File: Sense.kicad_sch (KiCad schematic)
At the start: 35 parts, among them J1 22-28-8083, J2 1x3 pin vertical, J3 1x3 pin vertical, J4 1x3 pin vertical, J5 1x3 pin vertical, P1 5KEV-0, P2 5KEV-0, T1 NSI50010YT1G, U1 INA226

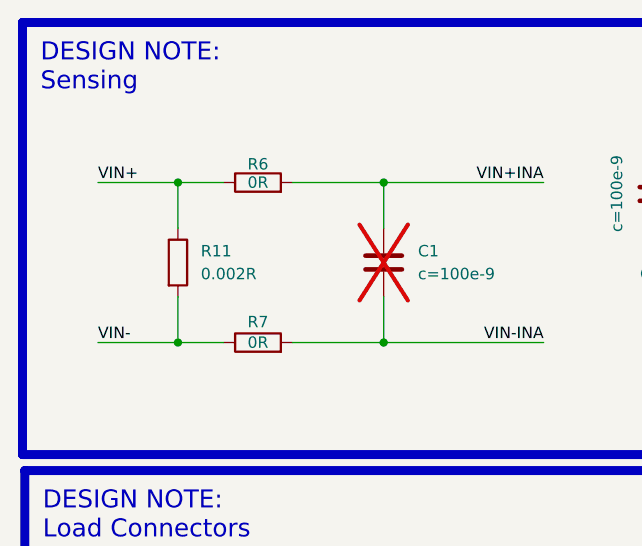
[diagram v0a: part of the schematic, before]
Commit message: Changed sense resistor and fixed connector position
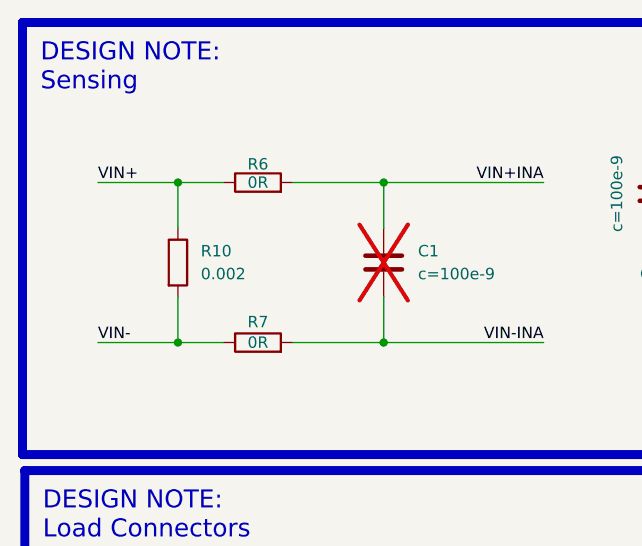
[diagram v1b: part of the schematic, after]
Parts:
- removed R11: 0.002R, Resistor_SMD:R_0805_2012Metric_Pad1.20x1.40mm_HandSolder, symbol 0_resistors:PMR10EZPFV2L00
- added R10: 0.002, Resistor_SMD:R_1206_3216Metric_Pad1.30x1.75mm_HandSolder, symbol 0_resistors:WSL12062L000FEA
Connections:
- net VIN+: now also R10.1
- net VIN-: now also R10.2
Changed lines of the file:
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@@
 			"AAAAAAAAAAAAAAAAAAAAAAAAAAAAAAAAAAAAAAAAAAAAAAAAAAAAAAAAAAAAAAAAAAAAAAAAAAAA"
 			"AAAAAAAAAAAAAAAAAAAAAAAAAAAAAAAAAAAAAAAAAAAAAAAAAAAAAAAAAAAAAAAAAAAAAAAAAAAA"
+			"AAAAAAAAAAAAAAAAAAAAAAAAAAAAAAAAAAAAAAAAAAAAAAAAAAAAAAAAAAAAAAAAAAAAAAAAAAAA"
+			"AAAAAAAAAAAAAAAAAAAAAAAAAAAAAAAAAAAAAAAAAAAAAAAAAAAAAAAAAAAAAAAAAAAAAAAAAAAA"
+			"AAAAAAAAAAAAAAAAAAAAAAAAAAAAAAAAAAAAAAAAAAAAAAAAAAAAAAAAAAAAAAAAAAAAAAAAAAAA"
+			"AAAAAAAAAAAAAAAAAAAAAAAAAAAAAAAAAAAAAAAAAAAAAAAAAAAAAAAAAAAAAAAAAAAAAAAAAAAA"
+			"AAAAAAAAAAAAAAAAAAAAAAAAAAAAAAAAAAAAAAAAAAAAAAAAAAAAAAAAAAAAAAAAAAAAAAAAAAAA"
+			"AAAAAAAAAAAAAAAAAAAAAAAAAAAAAAAAAAAAAAAAAAAAAAAAAAAAAAAAAAAAAAAAAAAAAAAAAAAA"
+			"AAAAAAAAAAAAAAAAAAAAAAAAAAAAAAAAAAAAAAAAAAAAAAAAAAAAAAAAAAAAAAAAAAAAAAAAAAAA"
+			"AAAAAAAAAAAAAAAAAAAAAAAAAAAAAAAAAAAAAAAAAAAAAAAAAAAAAAAAAAAAAAAAAAAAAAAAAAAA"
+			"AAAAAAAAAAAAAAAAAAAAAAAAAAAAAAAAAAAAAAAAAAAAAAAAAAAAAAAAAAAAAAAAAAAAAAAAAAAA"
+			"AAAAAAAAAAAAAAAAAAAAAAAAAAAAAAAAAAAAAAAAAAAAAAAAAAAAAAAAAAAAAAAAAAAAAAAAAAAA"
+			"AAAAAAAAAAAAAAAAAAAAAAAAAAAAAAAAAAAAAAAAAAAAAAAAAAAAAAAAAAAAAAAAAAAAAAAAAAAA"
+			"AAAAAAAAAAAAAAAAAAAAAAAAAAAAAAAAAAAAAAAAAAAAAAAAAAAAAAAAAAAAAAAAAAAAAAAAAAAA"
+			"AAAAAAAAAAAAAAAAAAAAAAAAAAAAAAAAAAAAAAAAAAAAAAAAAAAAAAAAAAAAAAAAAAAAAAAAAAAA"
+			"AAAAAAAAAAAAAAAAAAAAAAAAAAAAAAAAAAAAAAAAAAAAAAAAAAAAAAAAAAAAAAAAAAAAAAAAAAAA"
+			"AAAAAAAAAAAAAAAAAAAAAAAAAAAAAAAAAAAAAAAAAAAAAAAAAAAAAAAAAAAAAAAAAAAAAAAAAAAA"
+			"AAAAAAAAAAAAAAAAAAAAAAAAAAAAAAAAAAAAAAAAAAAAAAAAAAAAAAAAAAAAAAAAAAAAAAAAAAAA"
+			"AAAAAAAAAAAAAAAAAAAAAAAAAAAAAAAAAAAAAAAAAAAAAAAAAAAAAAAAAAAAAAAAAAAAAAAAAAAA"
+			"AAAAAAAAAAAAAAAAAAAAAAAAAAAAAAAAAAAAAAAAAAAAAAAAAAAAAAAAAAAAAAAAAAAAAAAAAAAA"
 			"AAAAAAAAAAAAAAAAAAAAAAAAAAAAAA=="
 		)
@@
 	)
 	(symbol
+		(lib_id "0_resistors:WSL12062L000FEA")
+		(at 31.75 40.64 0)
+		(unit 1)
+		(exclude_from_sim no)
+		(in_bom yes)
+		(on_board yes)
+		(dnp no)
+		(fields_autoplaced yes)
+		(property "Reference" "R10"
+			(at 34.29 39.3699 0)
+			(effects
+				(font
+					(size 1.27 1.27)
+				)
+				(justify left)
+			)
+		)
+		(property "Value" "0.002"
+			(at 34.29 41.9099 0)
+			(effects
+				(font
+					(size 1.27 1.27)
+				)
+				(justify left)
+			)
+		)
+		(property "Footprint" "Resistor_SMD:R_1206_3216Metric_Pad1.30x1.75mm_HandSolder"
+			(at 31.75 40.64 0)
+			(effects
+				(font
+					(size 1.27 1.27)
+				)
+				(hide yes)
+			)
+		)
+		(property "Datasheet" "https://www.vishay.com/doc?30100"
+			(at 31.75 40.64 0)
+			(effects
+				(font
+					(size 1.27 1.27)
+				)
+				(hide yes)
+			)
+		)
+		(property "Description" "Current Sense Resistor, 0.002R, 1206, SMD, 1/4watt, 1%"
+			(at 31.75 40.64 0)
+			(effects
+				(font
+					(size 1.27 1.27)
+				)
+				(hide yes)
+			)
+		)
+		(property "CompanyPN" ""
+			(at 31.75 40.64 0)
+			(effects
+				(font
+					(size 1.27 1.27)
+				)
+				(hide yes)
+			)
+		)
+		(property "Manufacturer Part Number" "WSL12062L000FEA"
+			(at 31.75 40.64 0)
+			(effects
+				(font
+					(size 1.27 1.27)
+				)
+				(hide yes)
+			)
+		)
+		(property "Sim.Device" "R"
+			(at 31.75 40.64 0)
+			(effects
+				(font
+					(size 1.27 1.27)
+				)
+				(hide yes)
+			)
+		)
+		(property "Sim.Pins" "1=+ 2=-"
+			(at 31.75 40.64 0)
+			(effects
+				(font
+					(size 1.27 1.27)
+				)
+				(hide yes)
+			)
+		)
+		(pin "2"
+		)
+		(pin "1"
+		)
+		(instances
+			(project ""
+				(path "/0650c7a8-acba-429c-9f8e-eec0baf0bc1c/fede4c36-00cc-4d3d-b71c-5243ba232202/7d5a1283-086b-46b0-8df7-a9850521fb5e"
+					(reference "R10")
+					(unit 1)
+				)
+			)
+		)
+	)
+	(symbol
 		(lib_id "power:VCC")
 		(at 246.38 115.57 0)
@@
 					(unit 1)
 				)
-			)
-		)
-	)
-	(symbol
-		(lib_id "0_resistors:PMR10EZPFV2L00")
-		(at 31.75 40.64 0)
-		(unit 1)
-		(exclude_from_sim no)
-		(in_bom yes)
-		(on_board yes)
-		(dnp no)
-		(fields_autoplaced yes)
-		(property "Reference" "R11"
-			(at 34.29 39.3699 0)
-			(effects
-				(font
-					(size 1.27 1.27)
-				)
-				(justify left)
-			)
-		)
-		(property "Value" "0.002R"
-			(at 34.29 41.9099 0)
-			(effects
-				(font
-					(size 1.27 1.27)
-				)
-				(justify left)
-			)
-		)
-		(property "Footprint" "Resistor_SMD:R_0805_2012Metric_Pad1.20x1.40mm_HandSolder"
-			(at 31.75 40.64 0)
-			(effects
-				(font
-					(size 1.27 1.27)
-				)
-				(hide yes)
-			)
-		)
-		(property "Datasheet" "https://fscdn.rohm.com/en/products/databook/datasheet/passive/resistor/chip_resistor/pmr_series-e.pdf"
-			(at 31.75 40.64 0)
-			(effects
-				(font
-					(size 1.27 1.27)
-				)
-				(hide yes)
-			)
-		)
-		(property "Description" "RESISTOR, 0.002R, 1%, 1/2W 0805"
-			(at 31.75 40.64 0)
-			(effects
-				(font
-					(size 1.27 1.27)
-				)
-				(hide yes)
-			)
-		)
-		(property "CompanyPN" ""
-			(at 31.75 40.64 0)
-			(effects
-				(font
-					(size 1.27 1.27)
-				)
-				(hide yes)
-			)
-		)
-		(property "Sim.Pins" "1=+ 2=-"
-			(at 31.75 40.64 0)
-			(effects
-				(font
-					(size 1.27 1.27)
-				)
-				(hide yes)
-			)
-		)
-		(property "Manufacturer Parn Number" "PMR10EZPFV2L00"
-			(at 31.75 40.64 0)
-			(effects
-				(font
-					(size 1.27 1.27)
-				)
-				(hide yes)
-			)
-		)
-		(property "Sim.Device" "R"
-			(at 31.75 40.64 0)
-			(effects
-				(font
-					(size 1.27 1.27)
-				)
-				(hide yes)
-			)
-		)
-		(property "Sim.Params" "r=0.002"
-			(at 31.75 40.64 0)
-			(effects
-				(font
-					(size 1.27 1.27)
-				)
-				(hide yes)
-			)
-		)
-		(property "Manufacturer Part Number" "CRCW060333R0FKEA"
-			(at 31.75 40.64 0)
-			(effects
-				(font
-					(size 1.27 1.27)
-				)
-				(hide yes)
-			)
-		)
-		(pin "1"
-		)
-		(pin "2"
-		)
-		(instances
-			(project ""
-				(path "/0650c7a8-acba-429c-9f8e-eec0baf0bc1c/fede4c36-00cc-4d3d-b71c-5243ba232202/7d5a1283-086b-46b0-8df7-a9850521fb5e"
-					(reference "R11")
-					(unit 1)
-				)

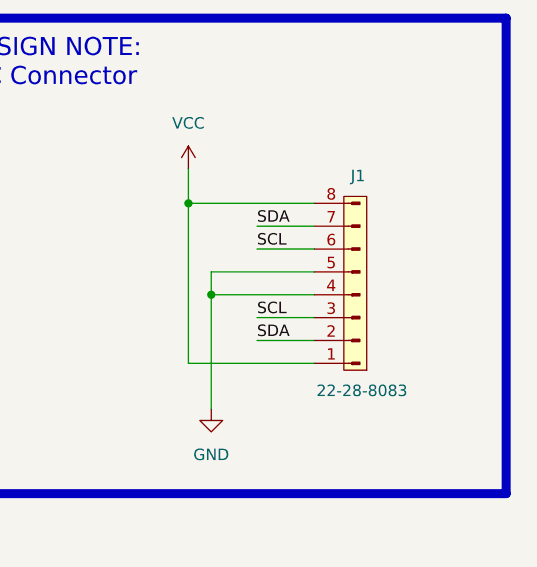
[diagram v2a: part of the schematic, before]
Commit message: Split I2C connector
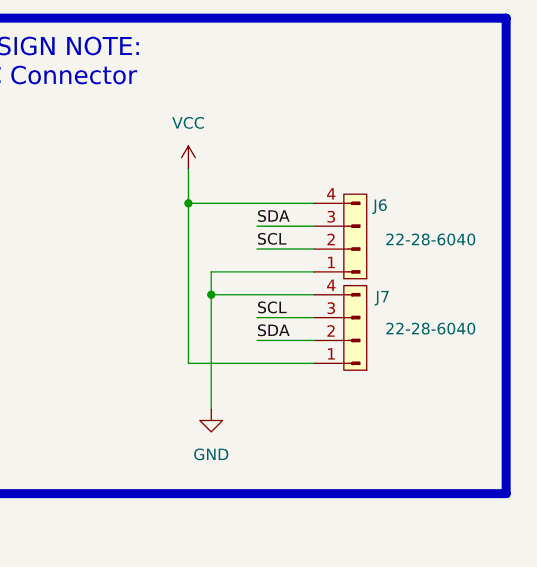
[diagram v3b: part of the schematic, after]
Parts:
- removed J1: 22-28-8083, Connector_PinHeader_2.54mm:PinHeader_1x08_P2.54mm_Horizontal, symbol 0_connectors:22-28-8083
- added J6, J7: 22-28-6040, Connector_PinHeader_2.54mm:PinHeader_1x04_P2.54mm_Horizontal, symbol 0_connectors:22-28-6040
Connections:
- net GND: now also J6.1 (Pin_1), J7.4 (Pin_4)
- net SCL: now also J6.2 (Pin_2), J7.3 (Pin_3)
- net SDA: now also J6.3 (Pin_3), J7.2 (Pin_2)
- net VCC: now also J6.4 (Pin_4), J7.1 (Pin_1)
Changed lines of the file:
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@@
 			"UDQuRjMyIHJlc3VsdC5wb3NpdGlvbi53LCB2ZXJ0ZXguYXR0cmliWzBdLCBjWzddOwpEUDQuRjMy"
 			"IHJlc3VsdC5wb3NpdGlvbi56LCB2ZXJ0ZXguYXR0cmliWzBdLCBjWzZdOwpFTkRJRjsKRU5ESUY7"
-			"CkVORElGOwpFTkRJRjsKRU5ESUY7Cg=="
+			"CkVORElGOwpFTkRJRjsKRU5ESUY7CgAAAAAAAAAAAAAAAAAAAAAAAAAAAAAAAAAAAAAAAAAAAAAA"
+			"AAAAAAAAAAAAAAAAAAAAAAAAAAAAAAAAAAAAAAAAAAAAAAAAAAAAAAAAAAAAAAAAAAAAAAAAAAAA"
+			"AAAAAAAAAAAAAAAAAAAAAAAAAAAAAAAAAAAAAAAAAAAAAAAAAAAAAAAAAAAAAAAAAAAAAAAAAAAA"
+			"AAAAAAAAAAAAAAAAAAAAAAAAAAAAAAAAAAAAAAAAAAAAAAAAAAAAAAAAAAAAAAAAAAAAAAAAAAAA"
+			"AAAAAAAAAAAAAAAAAAAAAAAAAAAAAAAAAAAAAAAAAAAAAAAAAAAAAAAAAAAAAAAAAAAAAAAAAAAA"
+			"AAAAAAAAAAAAAAAAAAAAAAAAAAAAAAAAAAAAAAAAAAAAAAAAAAAAAAAAAAAAAAAAAAAAAAAAAAAA"
+			"AAAAAAAAAAAAAAAAAAAAAAAAAAAAAAAAAAAAAAAAAAAAAAAAAAAAAAAAAAAAAAAAAAAAAAAAAAAA"
+			"AAAAAAAAAAAAAAAAAAAAAAAAAAAAAAAAAAAAAAAAAAAAAAAAAAAAAAAAAAAAAAAAAAAAAAAAAAAA"
+			"AAAAAAAAAAAAAAAAAAAAAAAAAAAAAAAAAAAAAAAAAAAAAAAAAAAAAAAAAAAAAAAAAAAAAAAAAAAA"
+			"AAAAAAAAAAAAAAAAAAAAAAAAAAAAAAAAAAAAAAAAAAAAAAAAAAAAAAAAAAAAAAAAAAAAAAAAAAAA"
+			"AAAAAAAAAAAAAAAAAAAAAAAAAAAAAAAAAAAAAAAAAAAAAAAAAAAAAAAAAAAAAAAAAAAAAAAAAAAA"
+			"AAAAAAAAAAAAAAAAAAAAAAAAAAAAAAAAAAAAAAAAAAAAAAAAAAAAAAAAAAAAAAAAAAAAAAAAAAAA"
+			"AAAAAAAAAAAAAAAAAAAAAAAAAAAAAAAAAAAAAAAAAAAAAAAAAAAAAAAAAAAAAAAAAAAAAAAAAAAA"
+			"AAAAAAAAAAAAAAAAAAAAAAAAAAAAAAAAAAAAAAAAAAAAAAAAAAAAAAAAAAAAAAAAAAAAAAAAAAAA"
+			"AAAAAAAAAAAAAAAAAAAAAAAAAAAAAAAAAAAAAAAAAAAAAAAAAAAAAAAAAAAAAAAAAAAAAAAAAAAA"
+			"AAAAAAAAAAAAAAAAAAAAAAAAAAAAAAAAAAAAAAAAAAAAAAAAAAAAAAAAAAAAAAAAAAAAAAAAAAAA"
+			"AAAAAAAAAAAAAAAAAAAAAAAAAAAAAAAAAAAAAAAAAAAAAAAAAAAAAAAAAAAAAAAAAAAAAAAAAAAA"
+			"AAAAAAAAAAAAAAAAAAAAAAAAAAAAAAAAAAAAAAAAAAAAAAAAAAAAAAAAAAAAAAAAAAAAAAAAAAAA"
+			"AAAAAAAAAAAAAAAAAAAAAAAAAAAAAA=="
 		)
 	)
@@
 	)
 	(symbol
-		(lib_id "0_connectors:22-28-8083")
-		(at 265.43 139.7 180)
-		(unit 1)
-		(exclude_from_sim no)
-		(in_bom yes)
-		(on_board yes)
-		(dnp no)
-		(property "Reference" "J1"
-			(at 264.414 116.332 0)
-			(effects
-				(font
-					(size 1.27 1.27)
-				)
-				(justify right)
-			)
-		)
-		(property "Value" "22-28-8083"
-			(at 260.604 140.208 0)
-			(effects
-				(font
-					(size 1.27 1.27)
-				)
-				(justify right)
-			)
-		)
-		(property "Footprint" "Connector_PinHeader_2.54mm:PinHeader_1x08_P2.54mm_Horizontal"
-			(at 265.43 139.7 0)
-			(effects
-				(font
-					(size 1.27 1.27)
-				)
-				(hide yes)
-			)
-		)
-		(property "Datasheet" "https://www.molex.com/en-us/products/part-detail/22288083?display=pdf"
-			(at 265.43 139.7 0)
-			(effects
-				(font
-					(size 1.27 1.27)
-				)
-				(hide yes)
-			)
-		)
-		(property "Description" "Headers & Wire Housings BKWY HDR R/A 8P 15AU"
-			(at 265.43 139.7 0)
-			(effects
-				(font
-					(size 1.27 1.27)
-				)
-				(hide yes)
-			)
-		)
-		(property "CompanyPN" ""
-			(at 265.43 139.7 0)
-			(effects
-				(font
-					(size 1.27 1.27)
-				)
-				(hide yes)
-			)
-		)
-		(property "Manufacturer Part Number" "22-28-8083"
-			(at 265.43 139.7 0)
-			(effects
-				(font
-					(size 1.27 1.27)
-				)
-				(hide yes)
-			)
-		)
-		(pin "8"
-		)
-		(pin "1"
-		)
-		(pin "3"
-		)
-		(pin "4"
-		)
-		(pin "2"
-		)
-		(pin "6"
-		)
-		(pin "5"
-		)
-		(pin "7"
-		)
-		(instances
-			(project ""
-				(path "/0650c7a8-acba-429c-9f8e-eec0baf0bc1c/fede4c36-00cc-4d3d-b71c-5243ba232202/7d5a1283-086b-46b0-8df7-a9850521fb5e"
-					(reference "J1")
-					(unit 1)
-				)
-			)
-		)
-	)
-	(symbol
 		(lib_id "power:GND")
 		(at 99.06 36.83 0)
@@
 	)
 	(symbol
+		(lib_id "0_connectors:22-28-6040")
+		(at 265.43 129.54 180)
+		(unit 1)
+		(exclude_from_sim no)
+		(in_bom yes)
+		(on_board yes)
+		(dnp no)
+		(property "Reference" "J6"
+			(at 267.716 119.634 0)
+			(effects
+				(font
+					(size 1.27 1.27)
+				)
+			)
+		)
+		(property "Value" "22-28-6040"
+			(at 273.304 123.444 0)
+			(effects
+				(font
+					(size 1.27 1.27)
+				)
+			)
+		)
+		(property "Footprint" "Connector_PinHeader_2.54mm:PinHeader_1x04_P2.54mm_Horizontal"
+			(at 265.43 129.54 0)
+			(effects
+				(font
+					(size 1.27 1.27)
+				)
+				(hide yes)
+			)
+		)
+		(property "Datasheet" "https://www.molex.com/en-us/products/part-detail-pdf/22286040?display=pdf"
+			(at 265.43 129.54 0)
+			(effects
+				(font
+					(size 1.27 1.27)
+				)
+				(hide yes)
+			)
+		)
+		(property "Description" "Headers & Wire Housings BKWY HDR STR 4P tin"
+			(at 265.43 129.54 0)
+			(effects
+				(font
+					(size 1.27 1.27)
+				)
+				(hide yes)
+			)
+		)
+		(property "CompanyPN" ""
+			(at 265.43 129.54 0)
+			(effects
+				(font
+					(size 1.27 1.27)
+				)
+				(hide yes)
+			)
+		)
+		(property "Manufacturer Part Number" "22-28-6040"
+			(at 265.43 129.54 0)
+			(effects
+				(font
+					(size 1.27 1.27)
+				)
+				(hide yes)
+			)
+		)
+		(pin "1"
+		)
+		(pin "4"
+		)
+		(pin "2"
+		)
+		(pin "3"
+		)
+		(instances
+			(project ""
+				(path "/0650c7a8-acba-429c-9f8e-eec0baf0bc1c/fede4c36-00cc-4d3d-b71c-5243ba232202/7d5a1283-086b-46b0-8df7-a9850521fb5e"
+					(reference "J6")
+					(unit 1)
+				)
+			)
+		)
+	)
+	(symbol
 		(lib_id "power:GND")
 		(at 143.51 124.46 0)
@@
 					(unit 1)
 				)
+			)
+		)
+	)
+	(symbol
+		(lib_id "0_connectors:22-28-6040")
+		(at 265.43 139.7 180)
+		(unit 1)
+		(exclude_from_sim no)
+		(in_bom yes)
+		(on_board yes)
+		(dnp no)
+		(property "Reference" "J7"
+			(at 267.97 129.794 0)
+			(effects
+				(font
+					(size 1.27 1.27)
+				)
+			)
+		)
+		(property "Value" "22-28-6040"
+			(at 273.304 133.35 0)
+			(effects
+				(font
+					(size 1.27 1.27)
+				)
+			)
+		)
+		(property "Footprint" "Connector_PinHeader_2.54mm:PinHeader_1x04_P2.54mm_Horizontal"
+			(at 265.43 139.7 0)
+			(effects
+				(font
+					(size 1.27 1.27)
+				)
+				(hide yes)
+			)
+		)
+		(property "Datasheet" "https://www.molex.com/en-us/products/part-detail-pdf/22286040?display=pdf"
+			(at 265.43 139.7 0)
+			(effects
+				(font
+					(size 1.27 1.27)
+				)
+				(hide yes)
+			)
+		)
+		(property "Description" "Headers & Wire Housings BKWY HDR STR 4P tin"
+			(at 265.43 139.7 0)
+			(effects
+				(font
+					(size 1.27 1.27)
+				)
+				(hide yes)
+			)
+		)
+		(property "CompanyPN" ""
+			(at 265.43 139.7 0)
+			(effects
+				(font
+					(size 1.27 1.27)
+				)
+				(hide yes)
+			)
+		)
+		(property "Manufacturer Part Number" "22-28-6040"
+			(at 265.43 139.7 0)
+			(effects
+				(font
+					(size 1.27 1.27)
+				)
+				(hide yes)
+			)
+		)
+		(pin "1"
+		)
+		(pin "4"
+		)
+		(pin "2"
+		)
+		(pin "3"
+		)
+		(instances
+			(project "KDT_Hierarchical"
+				(path "/0650c7a8-acba-429c-9f8e-eec0baf0bc1c/fede4c36-00cc-4d3d-b71c-5243ba232202/7d5a1283-086b-46b0-8df7-a9850521fb5e"
+					(reference "J7")
+					(unit 1)
+				)

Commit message: Outputs generated, ready for prototyping
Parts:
- added TP1, TP2, TP3: TestPoint, 0_testpoints:TestPoint_PTH_1mm_2mm, symbol Connector:TestPoint
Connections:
- net GND: now also TP3.1
- net VBUS: now also TP1.1
- net VCC: now also TP2.1
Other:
- moved on the sheet: FID1, FID2, H1, H2, H3, H4, R8, R9
